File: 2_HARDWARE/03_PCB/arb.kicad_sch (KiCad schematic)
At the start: 0 parts

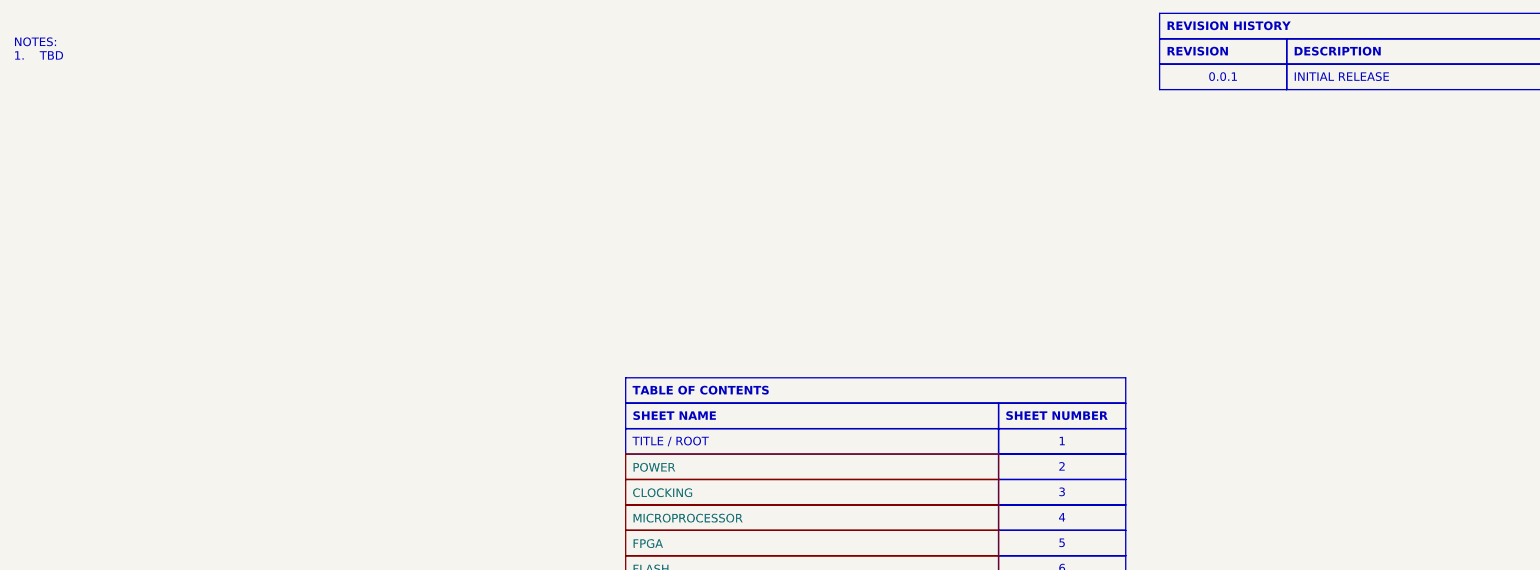
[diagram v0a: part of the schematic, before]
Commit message: MINOR: Adjusted soldermask and ported Schematic + PCB to Kicad 9.0.
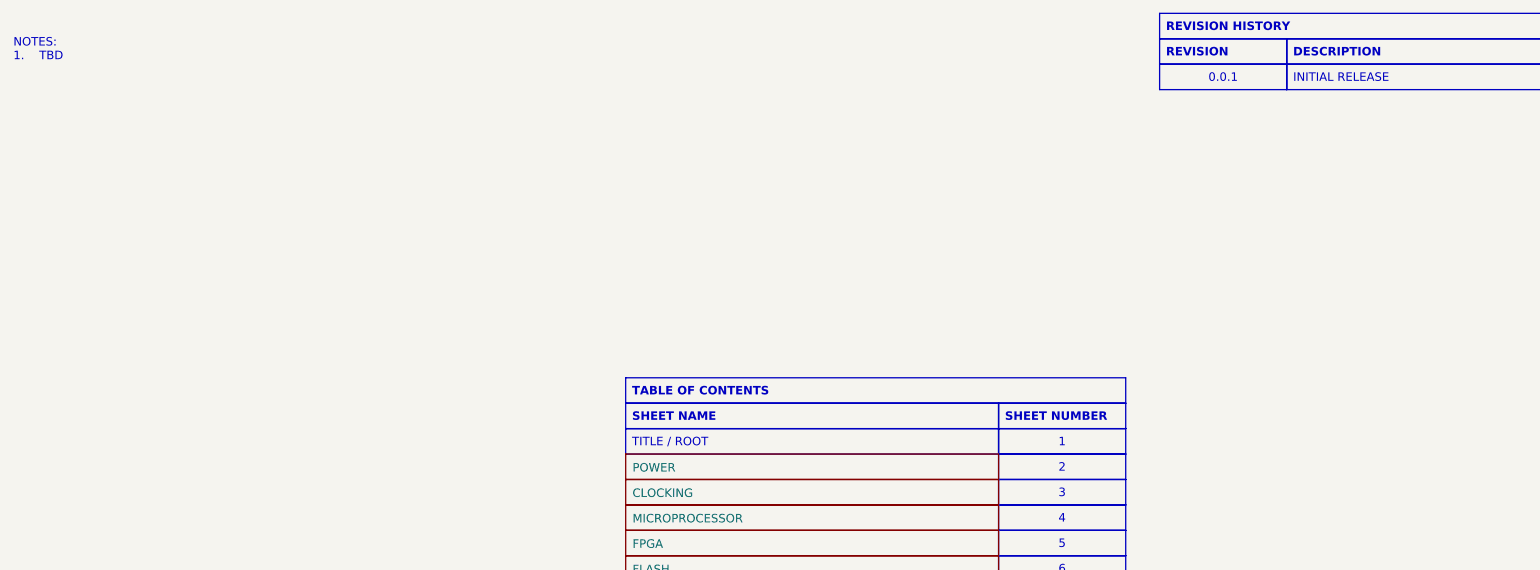
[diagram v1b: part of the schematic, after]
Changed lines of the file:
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@@
 (kicad_sch
-	(version 20231120)
+	(version 20250114)
 	(generator "eeschema")
-	(generator_version "8.0")
+	(generator_version "9.0")
 	(paper "A")
 	(title_block
@@
 		(company "Tomasz Brzyzek")
 	)
+	(text "NOTE: USED TO COPY & PASTE A BLANK HIERARCHAL SCHEMATIC SHEET."
+		(exclude_from_sim no)
+		(at 144.018 213.106 0)
+		(effects
+			(font
+				(size 1.27 1.27)
+			)
+		)
+	)
 	(text_box "2"
 		(exclude_from_sim no)
 		(at 165.1 81.28 0)
 		(size 19.05 3.81)
+		(margins 0.9525 0.9525 0.9525 0.9525)
 		(stroke
 			(width 0)
@@
 		(at 189.23 19.05 0)
 		(size 19.05 3.81)
+		(margins 0.9525 0.9525 0.9525 0.9525)
 		(stroke
 			(width 0)
@@
 		(at 165.1 85.09 0)
 		(size 19.05 3.81)
+		(margins 0.9525 0.9525 0.9525 0.9525)
 		(stroke
 			(width 0)
@@
 		(at 189.23 15.24 0)
 		(size 74.93 3.81)
+		(margins 0.9525 0.9525 0.9525 0.9525)
 		(stroke
 			(width 0)
@@
 		(at 165.1 88.9 0)
 		(size 19.05 3.81)
+		(margins 0.9525 0.9525 0.9525 0.9525)
 		(stroke
 			(width 0)
@@
 		(at 109.22 73.66 0)
 		(size 55.88 3.81)
+		(margins 0.9525 0.9525 0.9525 0.9525)
 		(stroke
 			(width 0)
@@
 		(at 109.22 69.85 0)
 		(size 74.93 3.81)
+		(margins 0.9525 0.9525 0.9525 0.9525)
 		(stroke
 			(width 0)
@@
 		(at 165.1 73.66 0)
 		(size 19.05 3.81)
+		(margins 0.9525 0.9525 0.9525 0.9525)
 		(stroke
 			(width 0)
@@
 		(at 165.1 100.33 0)
 		(size 19.05 3.81)
+		(margins 0.9525 0.9525 0.9525 0.9525)
 		(stroke
 			(width 0)
@@
 		(at 165.1 104.14 0)
 		(size 19.05 3.81)
+		(margins 0.9525 0.9525 0.9525 0.9525)
 		(stroke
 			(width 0)
@@
 		(at 165.1 115.57 0)
 		(size 19.05 3.81)
+		(margins 0.9525 0.9525 0.9525 0.9525)
 		(stroke
 			(width 0)
@@
 		(at 208.28 19.05 0)
 		(size 55.88 3.81)
+		(margins 0.9525 0.9525 0.9525 0.9525)
 		(stroke
 			(width 0)
@@
 		(at 165.1 96.52 0)
 		(size 19.05 3.81)
+		(margins 0.9525 0.9525 0.9525 0.9525)
 		(stroke
 			(width 0)
@@
 		(at 16.51 17.78 0)
 		(size 83.82 107.95)
+		(margins 0.9524 0.9524 0.9524 0.9524)
 		(stroke
 			(width -0.0001)
@@
 		(at 109.22 77.47 0)
 		(size 55.88 3.81)
+		(margins 0.9525 0.9525 0.9525 0.9525)
 		(stroke
 			(width 0)
@@
 		(at 165.1 111.76 0)
 		(size 19.05 3.81)
+		(margins 0.9525 0.9525 0.9525 0.9525)
 		(stroke
 			(width 0)
@@
 		(at 208.28 22.86 0)
 		(size 55.88 3.81)
+		(margins 0.9525 0.9525 0.9525 0.9525)
 		(stroke
 			(width 0)
@@
 		(at 165.1 119.38 0)
 		(size 19.05 3.81)
+		(margins 0.9525 0.9525 0.9525 0.9525)
 		(stroke
 			(width 0)
@@
 		(at 189.23 22.86 0)
 		(size 19.05 3.81)
+		(margins 0.9525 0.9525 0.9525 0.9525)
 		(stroke
 			(width 0)
@@
 		(at 165.1 92.71 0)
 		(size 19.05 3.81)
+		(margins 0.9525 0.9525 0.9525 0.9525)
 		(stroke
 			(width 0)
@@
 		(at 165.1 77.47 0)
 		(size 19.05 3.81)
+		(margins 0.9525 0.9525 0.9525 0.9525)
 		(stroke
 			(width 0)
@@
 		(at 165.1 107.95 0)
 		(size 19.05 3.81)
-		(stroke
-			(width 0)
-			(type default)
-			(color 0 0 0 1)
-		)
-		(fill
-			(type none)
-		)
-		(effects
-			(font
-				(size 1.27 1.27)
-				(color 0 72 72 1)
-			)
-		)
-	)
-	(text "NOTE: USED TO COPY & PASTE A BLANK HIERARCHAL SCHEMATIC SHEET."
-		(exclude_from_sim no)
-		(at 144.018 213.106 0)
-		(effects
-			(font
-				(size 1.27 1.27)
+		(margins 0.9525 0.9525 0.9525 0.9525)
+		(stroke
+			(width 0)
+			(type default)
+			(color 0 0 0 1)
+		)
+		(fill
+			(type none)
+		)
+		(effects
+			(font
+				(size 1.27 1.27)
+				(color 0 72 72 1)
 			)
 		)
@@
 		(at 109.22 88.9)
 		(size 55.88 3.81)
+		(exclude_from_sim no)
+		(in_bom yes)
+		(on_board yes)
+		(dnp no)
 		(stroke
 			(width 0.1524)
@@
 		(at 109.22 92.71)
 		(size 55.88 3.81)
+		(exclude_from_sim no)
+		(in_bom yes)
+		(on_board yes)
+		(dnp no)
 		(stroke
 			(width 0.1524)
@@
 		(at 109.22 107.95)
 		(size 55.88 3.81)
+		(exclude_from_sim no)
+		(in_bom yes)
+		(on_board yes)
+		(dnp no)
 		(stroke
 			(width 0.1524)
@@
 		(at 109.22 81.28)
 		(size 55.88 3.81)
+		(exclude_from_sim no)
+		(in_bom yes)
+		(on_board yes)
+		(dnp no)
 		(stroke
 			(width 0.1524)
@@
 		(at 109.22 96.52)
 		(size 55.88 3.81)
+		(exclude_from_sim no)
+		(in_bom yes)
+		(on_board yes)
+		(dnp no)
 		(stroke
 			(width 0.1524)
@@
 		(at 109.22 85.09)
 		(size 55.88 3.81)
+		(exclude_from_sim no)
+		(in_bom yes)
+		(on_board yes)
+		(dnp no)
 		(stroke
 			(width 0.1524)
@@
 		(at 109.22 100.33)
 		(size 55.88 3.81)
+		(exclude_from_sim no)
+		(in_bom yes)
+		(on_board yes)
+		(dnp no)
 		(stroke
 			(width 0.1524)
@@
 		(at 109.22 104.14)
 		(size 55.88 3.81)
+		(exclude_from_sim no)
+		(in_bom yes)
+		(on_board yes)
+		(dnp no)
 		(stroke
 			(width 0.1524)
@@
 		(at 109.22 214.63)
 		(size 55.88 3.81)
+		(exclude_from_sim no)
+		(in_bom yes)
+		(on_board yes)
+		(dnp no)
 		(stroke
 			(width 0.1524)
@@
 		(at 109.22 115.57)
 		(size 55.88 3.81)
+		(exclude_from_sim no)
+		(in_bom yes)
+		(on_board yes)
+		(dnp no)
 		(stroke
 			(width 0.1524)
@@
 		(at 109.22 111.76)
 		(size 55.88 3.81)
+		(exclude_from_sim no)
+		(in_bom yes)
+		(on_board yes)
+		(dnp no)
 		(stroke
 			(width 0.1524)
@@
 		(at 109.22 119.38)
 		(size 55.88 3.81)
+		(exclude_from_sim no)
+		(in_bom yes)
+		(on_board yes)
+		(dnp no)
 		(stroke
 			(width 0.1524)
@@
 		)
 	)
+	(embedded_fonts no)
 )
